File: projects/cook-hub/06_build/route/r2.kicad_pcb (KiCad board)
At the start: 4 copper layers, 185 x 120 mm, 182 parts, among them J1 EXT 5V 2A, J10 CONTACTOR 30V, J11 X9555WV 2x16 KEYPAD, J12 ENCODER DNP, J13 STEP/DIR/EN DNP, J14 SPARE I2C0+GP4, J15 MAX31865 DNP, J2 Pico 2 socket, J3 I2C0 MLX+SHT45, J4 I2C1 EXHAUST SHT45, J5 TC K-TYPE, J6 LOADCELL DIG, J7 DOOR NC+EOL, J8 E-STOP NC, J9 NTC x3, K1 DIP05-1A72-12L, K10 DIP05-1A72-12L, K11 DIP05-1A72-12L, K12 DIP05-1A72-12L, K13 DIP05-1A72-12L, K14 DIP05-1A72-12L, K15 DIP05-1A72-12L, K16 DIP05-1A72-12L, K2 DIP05-1A72-12L, K3 DIP05-1A72-12L, K4 DIP05-1A72-12L, K5 DIP05-1A72-12L, K6 DIP05-1A72-12L, K7 DIP05-1A72-12L, K8 DIP05-1A72-12L, K9 DIP05-1A72-12L, Q1 AO3401A hi-side, Q2 2N7002, Q3 AO3401A rev-prot, SW1 RUN reset, U1 MAX31856, U10 LTV-817S, U11 74HC14 E-stop, U12 AMS1117-3.3, U13 USBLC6-2SC6, U14 USBLC6-2SC6, U15 USBLC6-2SC6, U3 74HC595 #1, U4 74HC595 #2, U5 ULN2803A K1-K8, U6 ULN2803A K9-K16, U7 SN74LVC1G123, U8 74LVC1G00 /OE, U9 74LVC1G11 AND3

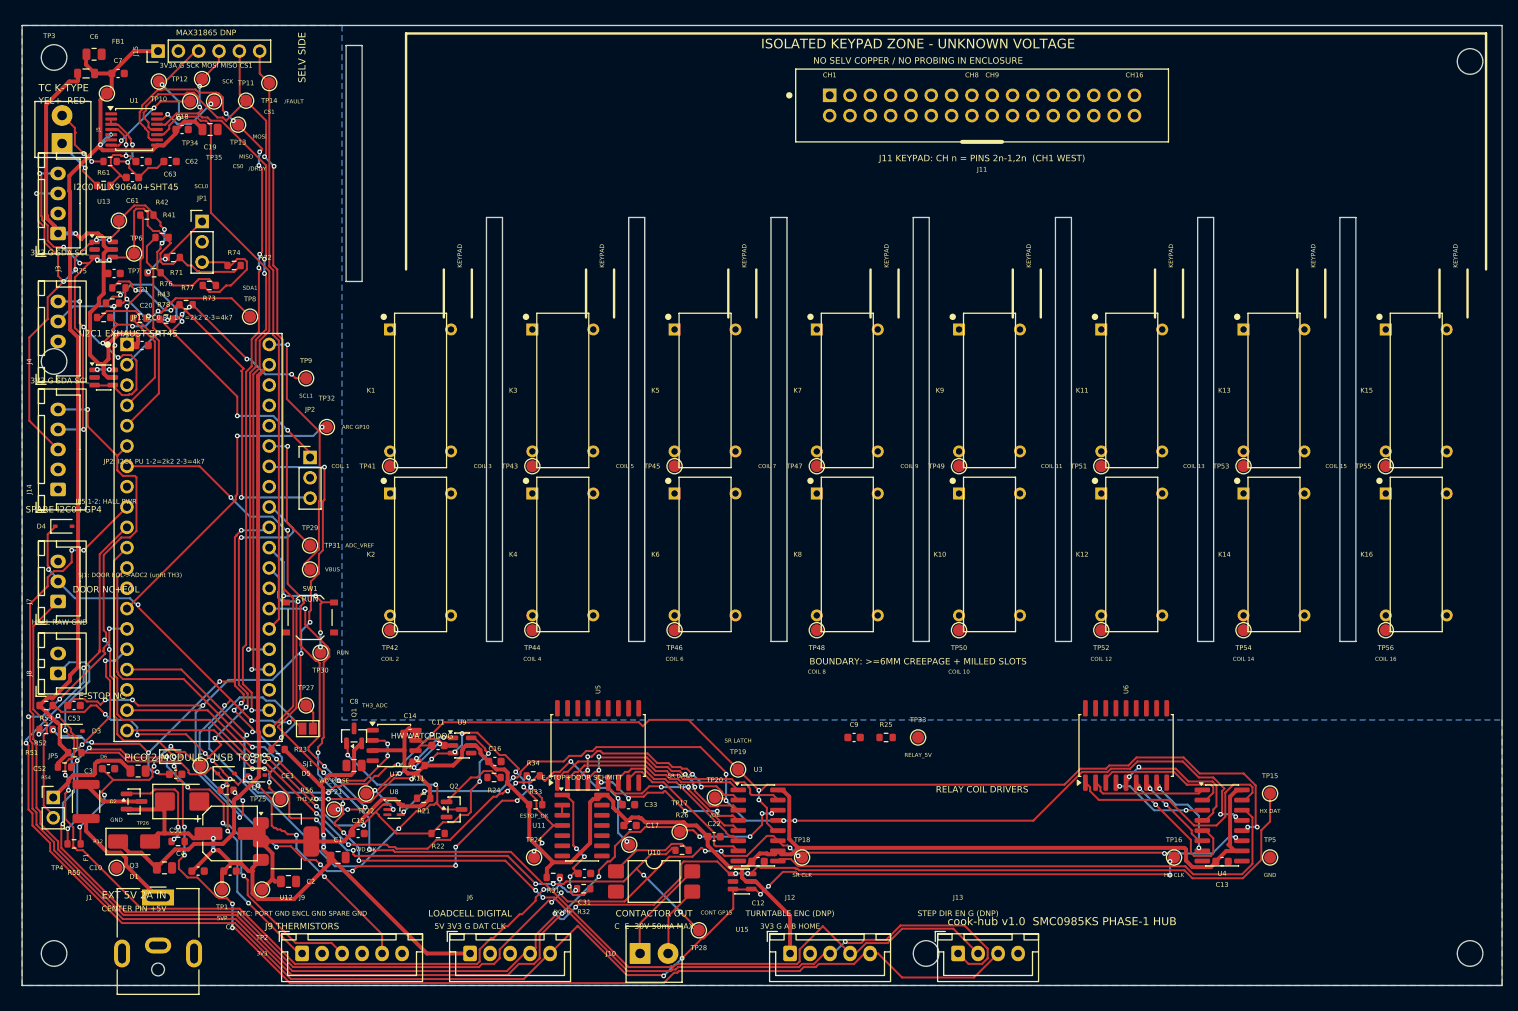
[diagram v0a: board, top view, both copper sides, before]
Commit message: cook-hub: WIP CHECKPOINT (not a gate) — electrical DRC bucket ELIMINATED (shorts/clearance/mask-bridge 16 -> 0)
Priority-1 fix from ADR-0006 diagnosis: the 6 shorts + 2 clearances + 8
solder-mask-bridges came from decoupler/RC parts pinned directly ONTO IC/
connector pads. Loosened the pins in generate_board.py ANCHOR (all still pass
the IP<=7mm proximity audit), re-routed the full chain:

- watchdog trio out of the U7 pad-field into the free pocket S/E of U7
  (NOGO y<=106.8 forbids N; U8 y117 bounds S): R11->(66.5,114.3) C14->(70,113.5)
  C11->(71.5,110,rot90). IP to U7: 4.3 / 4.95 / 5.0 mm.
- C21 (I2C1 ESD decoupler) was landing pad1 on J2 Pico pad1 (SDA0); moved N of
  its IC U14 -> (30.2,61), IP 3mm.
- U12 (AMS1117) +3mm E -> (56,122): its SOT-223 tab was shorting CE1 GND pad.
- H5 mounting hole (24,62) overlapped connector J4 (mask bridge x2); the west
  edge is fully packed with JST connectors, relocated to the y107-114 gap -> (24,110.5).

GND rescue (stitch_and_fill): added via-in-pad for GND SMD pads (In1 is a solid
GND plane; same-net barrel always bonds a boxed-in pad) + widened the U12 tab
thermal-via search; GND rescue is now non-fatal (DRC unconnected gate catches
genuine misses). Unconnected 64 -> 10.

audit_board I8: D6/R55 added to sanctioned refdes waivers (estop-divider tiny
0603/SOD passives, F.Fab copies, functional net silk nearby — same class as R56).
COST_ESTIMATE + ARCHITECTURE: board size 185x112 -> 185x120 (ADR-0006).

DRC now 480/10/1. NOT a gate: the elevated total vs the inherited 453 is stochastic
KRT route-quality from re-routing from scratch (track_width 45 = 5VP PWR-floor 0.5
thin-passes; via_dangling 32 = 5VP/3V3 F/B vias outside their In2 pours). Remaining
buckets untouched: silk 330 (deterministic), courtyards 44, holes 6, copper-edge 7.
Next: select/tune a clean route + promote (M3), silk de-collision campaign, courtyard
classification, DRU floors to JLC actuals (golden-rule-8).

Co-Authored-By: Claude Fable 5 <noreply@anthropic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
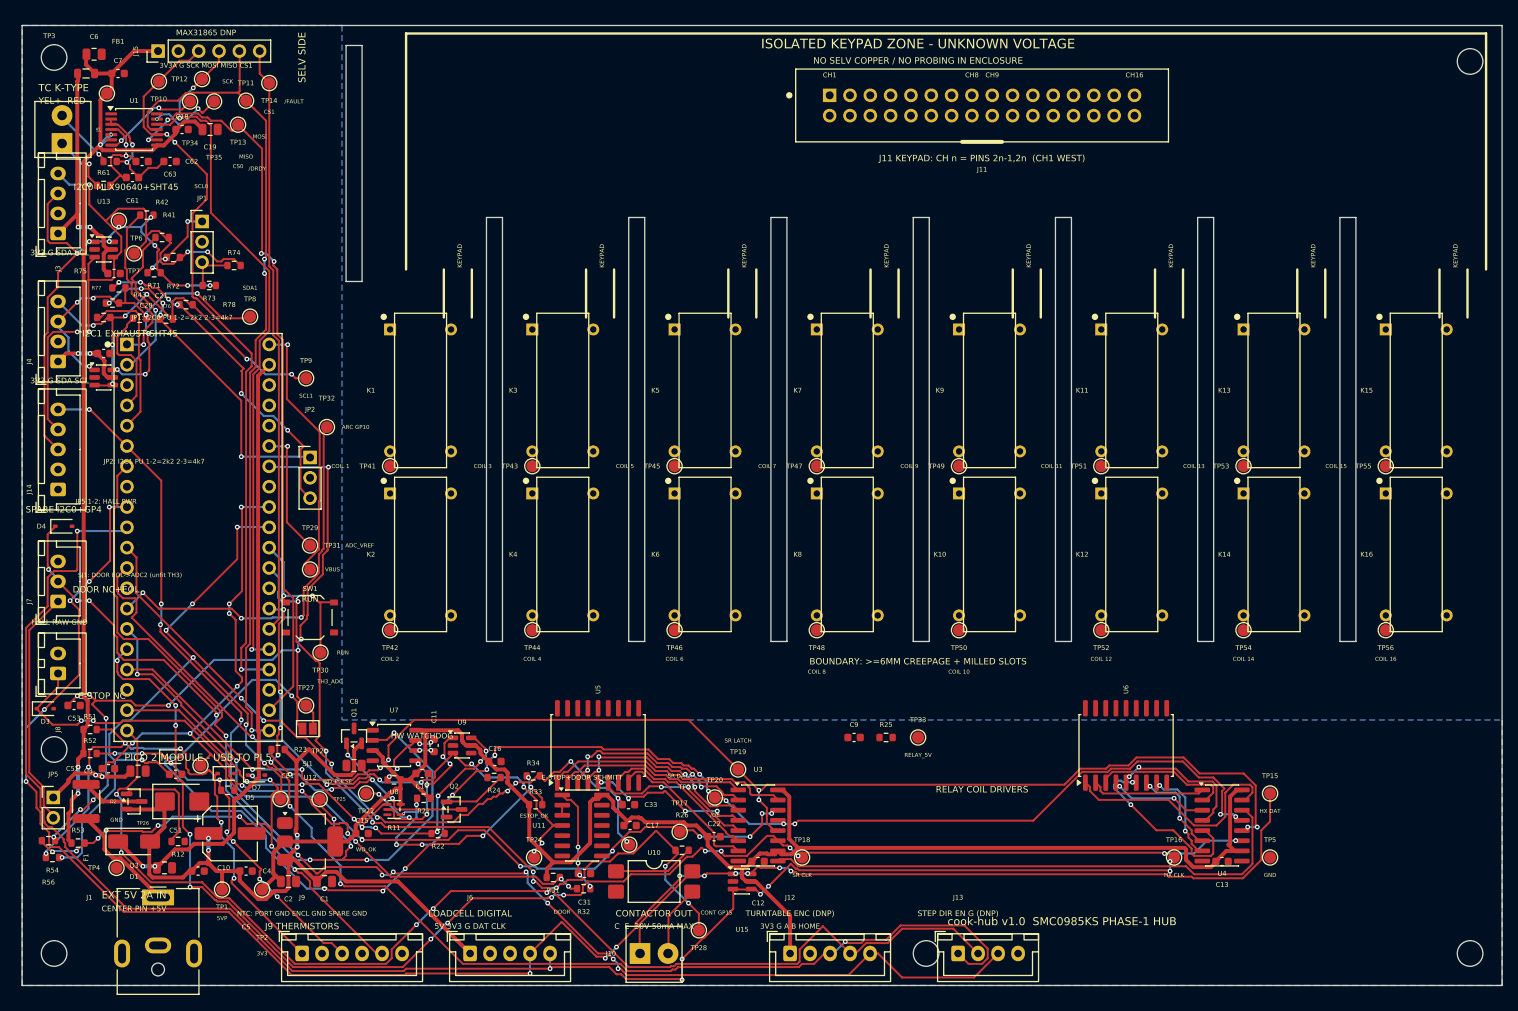
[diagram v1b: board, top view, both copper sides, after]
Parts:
- moved H5 48.5 mm to (24.0, 110.5)
- moved R56 23.2 mm to (23.3, 121.9)
- moved R55 20.3 mm to (45.7, 115.6)
- moved R53 17.7 mm to (27.0, 122.2)
- moved R54 16.0 mm to (23.8, 124.0)
- moved C14 5.22 mm to (70.0, 113.5)
- moved C21 4.90 mm to (30.2, 61.0)
- moved D3 4.56 mm to (22.9, 105.4)
- moved R52 3.62 mm to (28.5, 111.0)
- moved R11 3.50 mm to (66.5, 114.3)
- moved R51 3.47 mm to (28.5, 108.0)
- moved C1 3.45 mm to (57.8, 127.0)
- moved U12 3.00 mm to (56.0, 122.0)
- moved TP21 2.22 mm to (57.2, 116.7)
- moved C5 2.00 mm to (48.0, 125.7)
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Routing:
- net Q1G: track 78.7 -> 35.1 mm, vias 4 -> 5
- net SR_DATA: track 147.2 -> 104.9 mm
- net WD_PULSE: track 78.8 -> 106.5 mm, vias 9 -> 6
- net CONT_REQ: track 91.5 -> 114.4 mm
- net 3V3: track 287.6 -> 266.8 mm, vias 1 -> 6
- net ESTOP_RAW: track 106.0 -> 85.6 mm, vias 6 -> 8
- net GP4_SPARE: track 189.7 -> 170.8 mm, vias 9 -> 11
- net TH2: track 62.4 -> 45.9 mm, vias 7 -> 8
- net TH1_ADC: track 75.0 -> 90.6 mm, vias 10 -> 8
- net DOOR_IN: track 105.2 -> 91.7 mm
- net SR_CLK: track 194.9 -> 181.9 mm, vias 11 -> 15
- net DOOR_RAW: track 113.0 -> 125.5 mm, vias 13 -> 11
- net TH1: track 55.5 -> 66.7 mm, vias 4 -> 6
- net SDA1_J: track 40.2 -> 51.3 mm, vias 7 -> 8
- net WD_OK: track 18.4 -> 29.0 mm, vias 5 -> 7
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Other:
- board text removed: "TH1_ADC"

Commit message: cook-hub: WIP CHECKPOINT (not a gate) — mid zone-chamfer + COIL_EN work at 15/2/0; agent hit 529
Co-Authored-By: Claude Fable 5 <noreply@anthropic.com>
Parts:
- moved H6 13.9 mm to (126.0, 124.0)
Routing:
- net DOOR_RAW: track 125.5 -> 105.2 mm, vias 11 -> 9
- net ESTOP_RAW: track 85.6 -> 104.3 mm, vias 8 -> 7
- net CS0: track 92.8 -> 111.3 mm, vias 4 -> 2
- net FAULT_N: track 9.48 -> 27.1 mm
- net MISO: track 105.6 -> 122.6 mm, vias 3 -> 0
- net ESTOP_OK: track 84.0 -> 99.3 mm, vias 8 -> 10
- net SCL0_J: track 79.6 -> 66.7 mm, vias 5 -> 8
- net OE_N: track 136.8 -> 125.3 mm, vias 14 -> 13
- net SDA1_J: track 51.3 -> 40.1 mm, vias 8 -> 6
- net DRV14: track 23.9 -> 13.2 mm
- net ARC: track 49.1 -> 38.6 mm
- net HX_CLK: track 211.2 -> 201.0 mm, vias 8 -> 12
- net TH1: track 66.7 -> 74.1 mm, vias 6 -> 8
- net PU1_47: track 42.1 -> 49.3 mm, vias 6 -> 4
- net WD_PULSE: track 106.5 -> 100.0 mm, vias 6 -> 7
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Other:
- board text added: "3V3A"
- board text added: "SDA0"
- board text added: "TH1_ADC"
- board text added: "TH2_ADC"
- board text removed: "JP1: I2C0 PU 1-2=2k2 2-3=4k7"
- board text removed: "MAX31865 DNP"

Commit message: cook-hub v1.0 + cook-loadcell v1.0: SEALED releases (2026-07-19)
Both boards sealed at 07_releases/v1.0-2026-07-19/ with sha256 MANIFESTs,
ORDER_READMEs, fab packages (gerbers zip + coded BOM + CPL), pdf sets,
and verification evidence (twin report + renders, DRC gate json,
pin_review.md).

cook-hub v1.0 scoreboard: ERC 0 · parity 0 · DRC severity-all+refill
0/0/0 · AUDIT PASS (I-ISO 6.12mm, 8 slots) · policy FAIL=0 (14P/3W/6H) ·
twin exit 0 (219 checks, 0 unadjudicated criticals) · pin reviews 3/3
PASS · stock 82/82 >= 5x qty5 · render PASS-WITH-NOTES dispositioned.
ORDER_README: §16-condensed bring-up, Pico-2-NOT-included, §1.9 teardown
gate (no appliance hookup until donor keypad facts), §17 open items.

cook-loadcell v1.0 scoreboard: ERC 0 · parity 0 · DRC 0/0/0 (no DRC
waivers) · AUDIT PASS (I-AN 4mm guard) · policy FAIL=0 (8P/4W/7H) · twin
exit 0 (43 checks) · HX711 pin review PASS (E- float ship-blocker fixed;
AVDD 4.30V) · stock PASS · spec §3.7(a-g) mapping recorded in MANIFEST.
BOM well under the $20 target.

Loadcell policy waivers (R-POUR analog-nets, P-POL inline-asserts,
P-KEEP edge-mates, S-VER SS8550) + r0.kicad_pro netclass refresh.
Firmware skeletons (05_firmware: pinmap.h, COBS+CRC32 protocol.h +
PROTOCOL.md, relay_fsm.h fault hierarchy, watchdog.h) ship in-tree.

Co-Authored-By: Claude Fable 5 <noreply@anthropic.com>
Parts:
- U7: footprint Package_SO:SSOP-8_3.9x5.05mm_P1.27mm -> Package_SO:SSOP-8_2.95x2.8mm_P0.65mm
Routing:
- net GND: track 0.00 -> 116.7 mm, vias 0 -> 12
- net 3V3: track 269.6 -> 229.9 mm
- net COIL_EN: track 0.00 -> 11.5 mm, vias 0 -> 2
- net WD_RCX: track 9.81 -> 15.8 mm, vias 4 -> 2
- net DRDY_N: track 16.3 -> 21.7 mm, vias 2 -> 4
- net TC_P: track 13.6 -> 15.6 mm, vias 2 -> 3
- net TH1_ADC: track 91.7 -> 93.1 mm, vias 10 -> 9
- net PU1_22: track 44.3 -> 45.7 mm, vias 3 -> 6
- net TH2_ADC: track 64.0 -> 65.1 mm, vias 7 -> 6
- net WD_CX: track 2.45 -> 3.56 mm
- net WD_OK: track 25.4 -> 24.4 mm, vias 5 -> 4
- net WD_PULSE: track 100.0 -> 99.4 mm, vias 7 -> 8
